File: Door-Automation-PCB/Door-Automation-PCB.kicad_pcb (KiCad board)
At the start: 2 copper layers, 139.3 x 70.4 mm, 10 parts, among them J1 Conn_01x15_Female, J2 Conn_01x15_Female, J3 Screw_Terminal_01x01, J4 Screw_Terminal_01x01, J5 Screw_Terminal_01x02, J6 Screw_Terminal_01x02, J7 Screw_Terminal_01x02, U1 ESP32-DEVKIT-V1, U2 buck_converter, U3 buck_converter

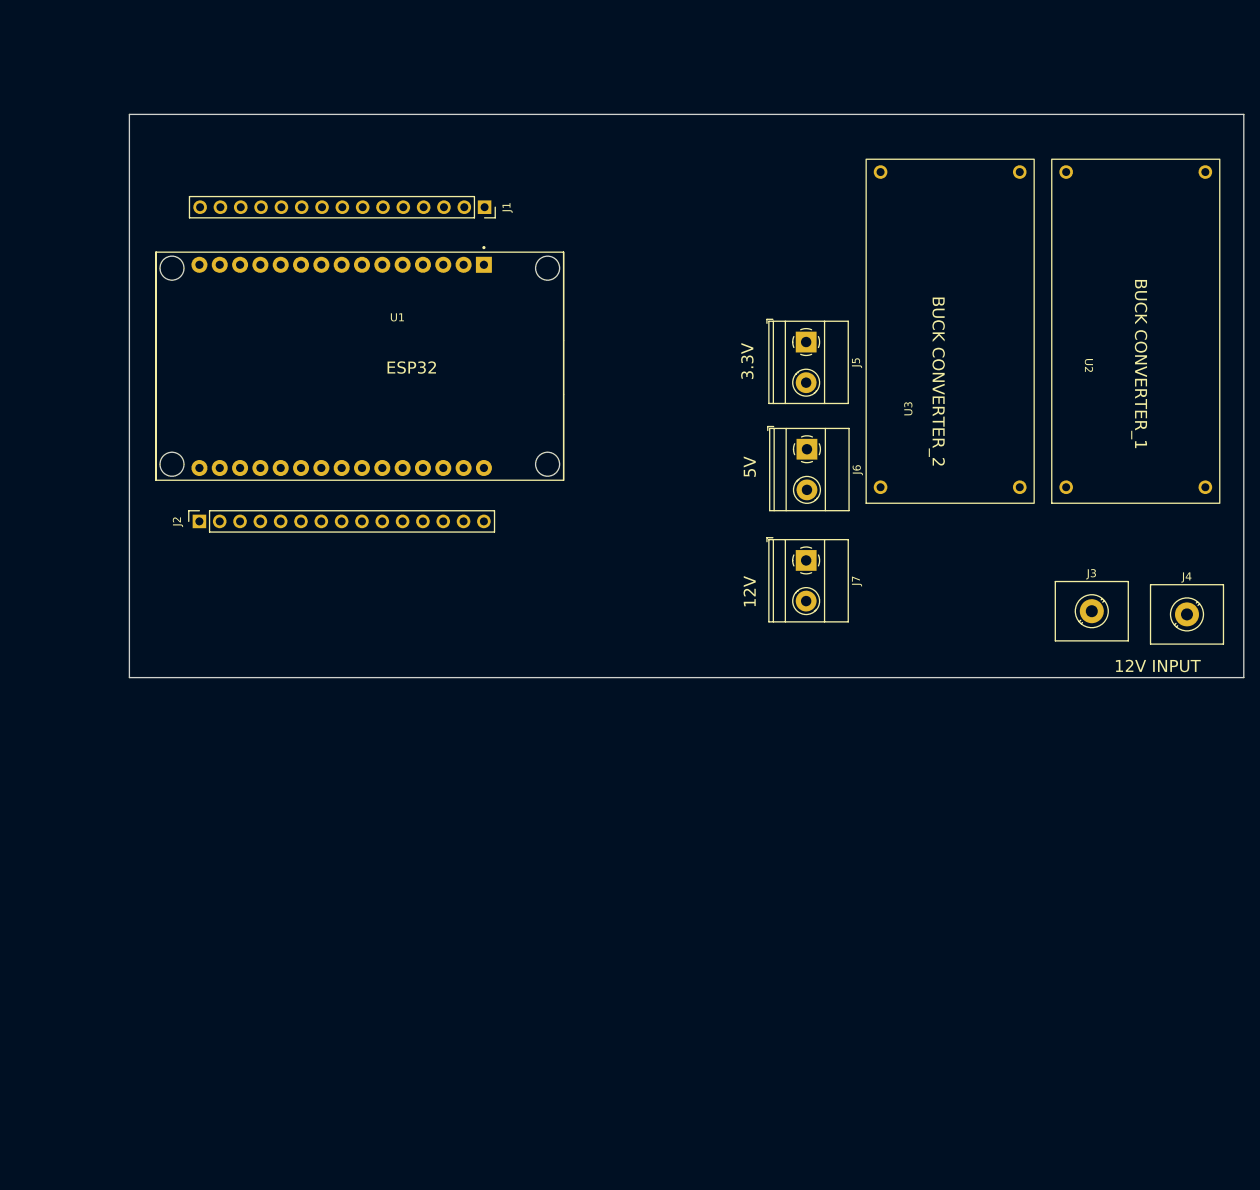
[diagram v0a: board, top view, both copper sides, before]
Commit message: added mosfet switch
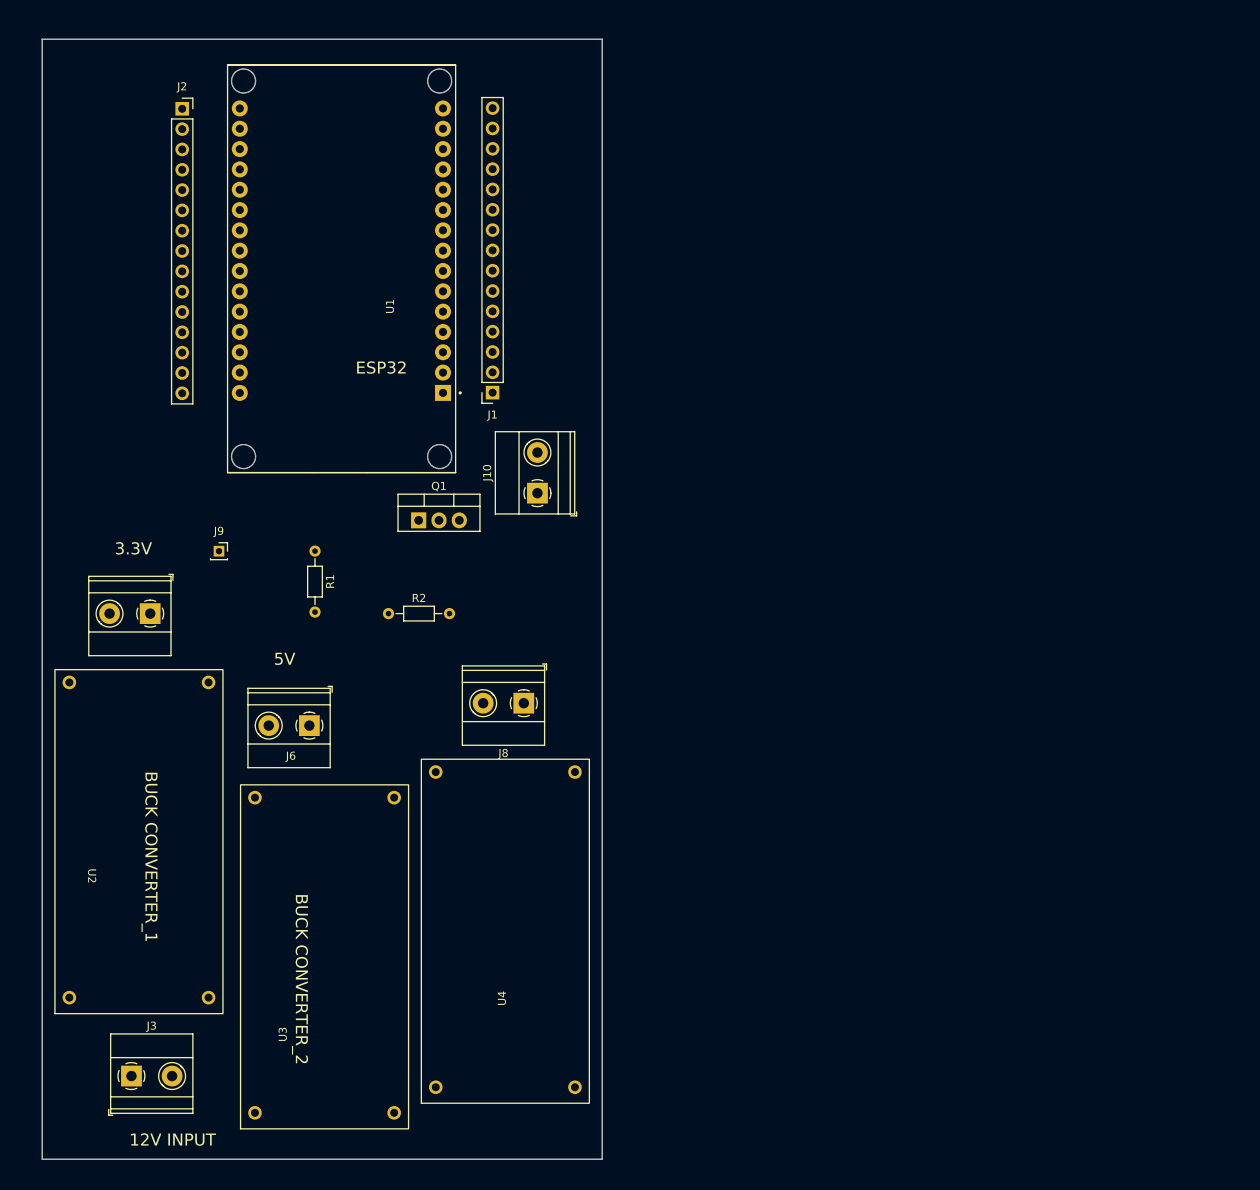
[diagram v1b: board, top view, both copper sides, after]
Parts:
- removed J4: Screw_Terminal_01x01, TerminalBlock_MetzConnect:TerminalBlock_MetzConnect_360271_1x01_Horizontal_ScrewM3.0_Boxed
- removed J7: Screw_Terminal_01x02, TerminalBlock_Phoenix:TerminalBlock_Phoenix_MKDS-1,5-2-5.08_1x02_P5.08mm_Horizontal
- added J10: Solenoid conn, TerminalBlock_Phoenix:TerminalBlock_Phoenix_MKDS-1,5-2-5.08_1x02_P5.08mm_Horizontal, F.Cu at (141.9, 96.7)
- added J8: 9V, TerminalBlock_Phoenix:TerminalBlock_Phoenix_MKDS-1,5-2-5.08_1x02_P5.08mm_Horizontal, F.Cu at (140.2, 123.0)
- added J9: D, Connector_PinSocket_2.00mm:PinSocket_1x01_P2.00mm_Vertical, F.Cu at (102.1, 104.0)
- added Q1: IRLZ34N, Package_TO_SOT_THT:TO-220-3_Vertical, F.Cu at (127.1, 100.1)
- added R1: 1K, Resistor_THT:R_Axial_DIN0204_L3.6mm_D1.6mm_P7.62mm_Horizontal, F.Cu at (114.1, 104.0)
- added R2: 1OK, Resistor_THT:R_Axial_DIN0204_L3.6mm_D1.6mm_P7.62mm_Horizontal, F.Cu at (123.3, 111.8)
- added U4: buck_converter, converters:buck_converter, F.Cu at (127.4, 173.0)
- J3: value Screw_Terminal_01x01 -> 12V_IN; footprint TerminalBlock_MetzConnect:TerminalBlock_MetzConnect_360271_1x01_Horizontal_ScrewM3.0_Boxed -> TerminalBlock_Phoenix:TerminalBlock_Phoenix_MKDS-1,5-2-5.08_1x02_P5.08mm_Horizontal
- J5: value Screw_Terminal_01x02 -> 3.3V
- J6: value Screw_Terminal_01x02 -> 5V
- moved U2 140.0 mm to (81.6, 161.8)
- moved J3 133.4 mm to (91.2, 169.6)
- moved U3 110.6 mm to (104.8, 176.2)
- moved J5 88.7 mm to (93.5, 111.8), turned to 180 degrees
- moved J6 71.1 mm to (113.4, 125.8), turned to 180 degrees
- moved J2 51.6 mm to (97.5, 48.7), turned to 0 degrees
- moved J1 23.2 mm to (136.3, 84.2), turned to 180 degrees
- moved U1 12.4 mm to (117.4, 68.7), turned to 180 degrees
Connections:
- net Net-(J5-Pad1) renamed /+3.3V
- net Net-(J6-Pad1) renamed /+5V
- J1 pad 2: Net-(J2-Pad14) -> /GND
- J2 pad 14: Net-(J2-Pad14) -> /GND
- J5 pad 2: Net-(J5-Pad2) -> /GND
- J6 pad 2: Net-(J5-Pad2) -> /GND
- U1 pad 2: Net-(J2-Pad14) -> /GND
- U1 pad 29: Net-(J2-Pad14) -> /GND
- U2 pad 1: Net-(J3-Pad1) -> Net-(J3-Pad2)
- U2 pad 2: Net-(J4-Pad1) -> Net-(J3-Pad1)
- U2 pad 4: Net-(J5-Pad2) -> /GND
- U3 pad 1: Net-(J3-Pad1) -> Net-(J3-Pad2)
- U3 pad 2: Net-(J4-Pad1) -> Net-(J3-Pad1)
- U3 pad 4: Net-(J5-Pad2) -> /GND
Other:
- board size 139.3 x 70.4 mm -> 70 x 140 mm
- board text removed: "12V"

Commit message: buck converter
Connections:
- J5 pad 1: /+3.3V -> /GND
- J5 pad 2: /GND -> /+3.3V
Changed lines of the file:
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@@
     (fp_circle (center 0 0) (end 1.5 0) (layer "F.Fab") (width 0.1) (fill none))
     (pad "1" thru_hole rect (at 0 0 180) (size 2.6 2.6) (drill 1.3) (layers *.Cu *.Mask)
-      (net 31 "/+3.3V") (pinfunction "Pin_1") (pintype "passive"))
+      (net 30 "/GND") (pinfunction "Pin_1") (pintype "passive"))
     (pad "2" thru_hole circle (at 5.08 0 180) (size 2.6 2.6) (drill 1.3) (layers *.Cu *.Mask)
-      (net 30 "/GND") (pinfunction "Pin_2") (pintype "passive"))
+      (net 31 "/+3.3V") (pinfunction "Pin_2") (pintype "passive"))
     (model "${KICAD6_3DMODEL_DIR}/TerminalBlock_Phoenix.3dshapes/TerminalBlock_Phoenix_MKDS-1,5-2-5.08_1x02_P5.08mm_Horizontal.wrl"
       (offset (xyz 0 0 0))

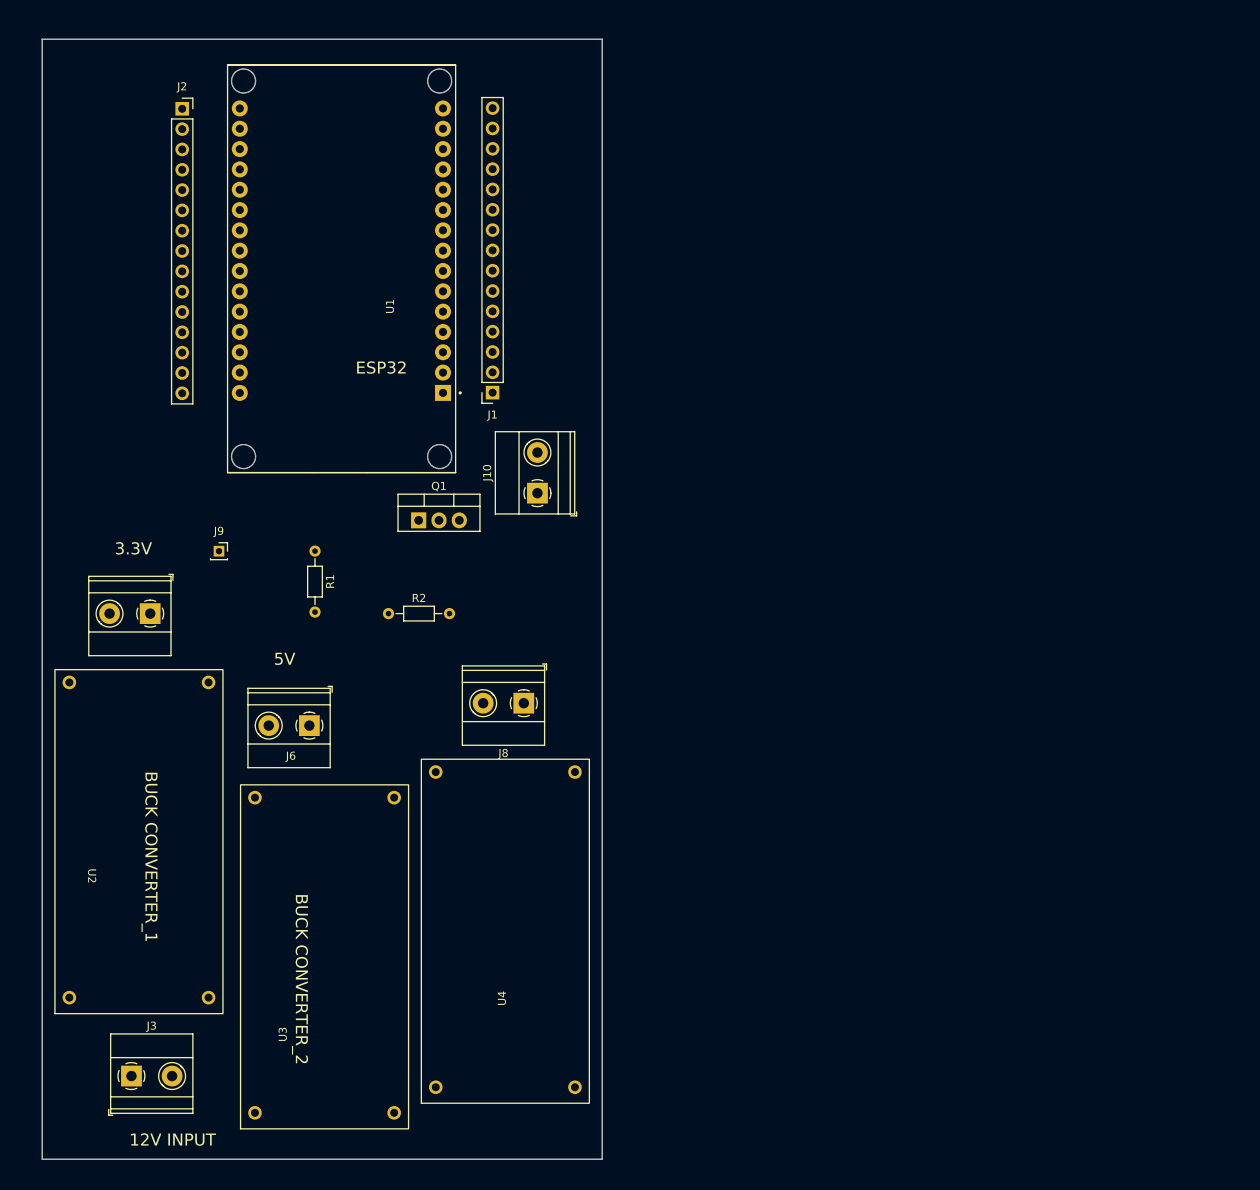
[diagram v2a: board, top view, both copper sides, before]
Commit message: added drill holes
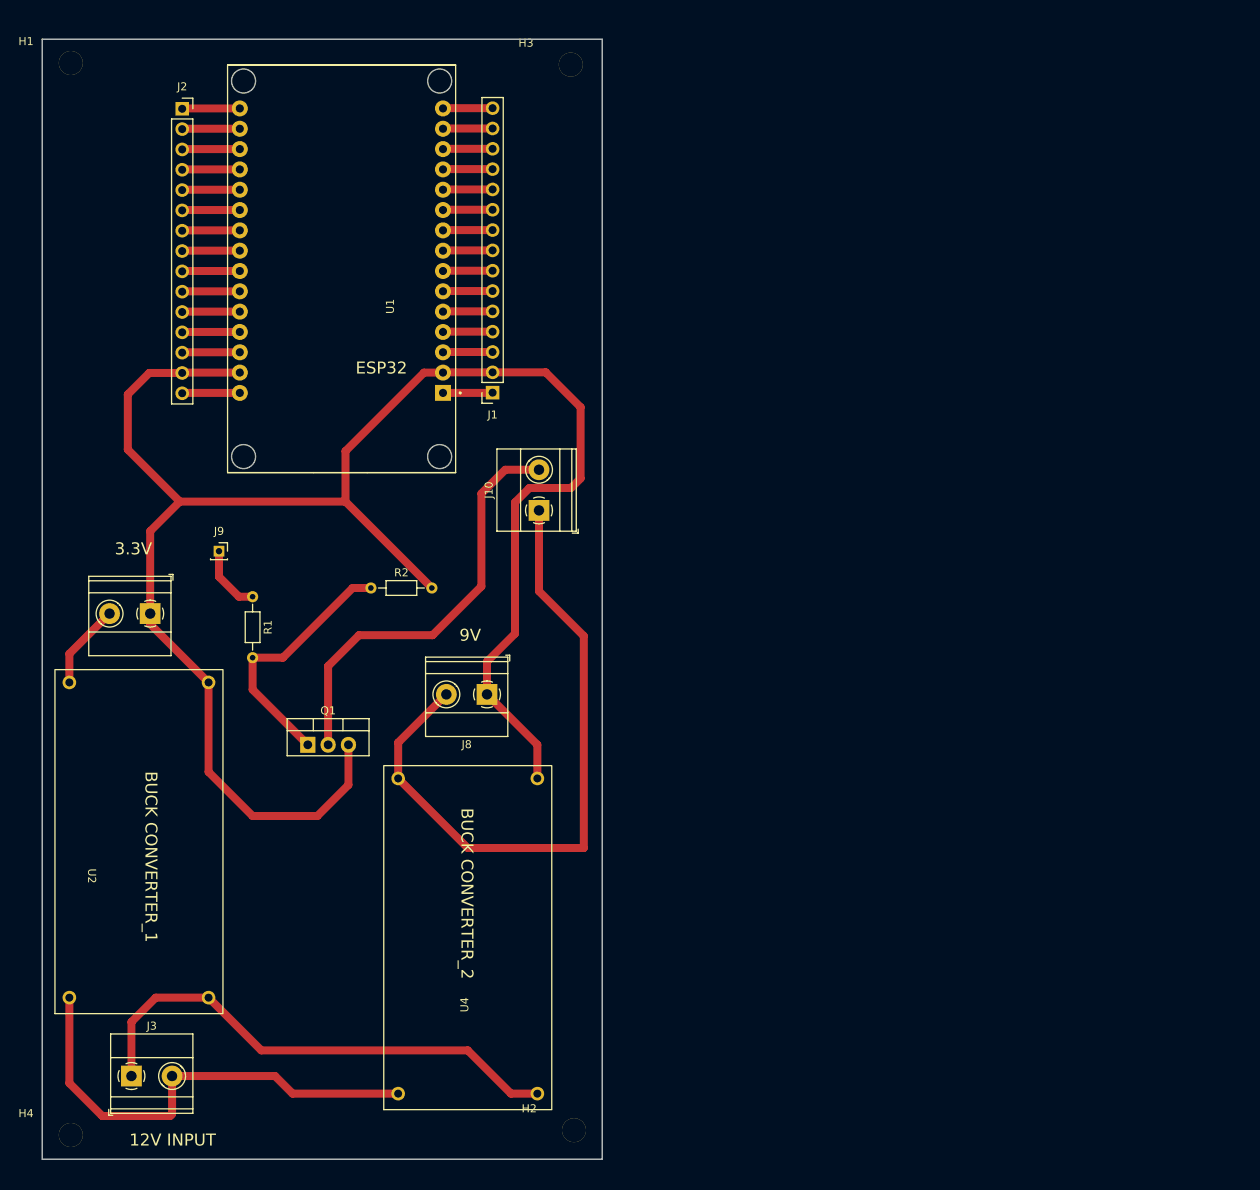
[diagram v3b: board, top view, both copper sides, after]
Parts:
- removed J6: 5V, TerminalBlock_Phoenix:TerminalBlock_Phoenix_MKDS-1,5-2-5.08_1x02_P5.08mm_Horizontal
- removed U3: buck_converter, converters:buck_converter
- added H1: hole, drill_hole:hole, F.Cu at (78.0, 40.8)
- added H2: hole, drill_hole:hole, F.Cu at (140.9, 174.2)
- added H3: hole, drill_hole:hole, F.Cu at (140.5, 41.0)
- added H4: hole, drill_hole:hole, F.Cu at (78.0, 174.8)
- moved Q1 31.3 mm to (113.2, 128.2)
- moved R1 9.66 mm to (106.3, 109.7)
- moved U4 4.77 mm to (122.7, 173.8)
- moved J8 4.73 mm to (135.6, 121.9)
- moved R2 3.88 mm to (121.1, 108.6)
- moved J10 2.16 mm to (142.1, 98.9)
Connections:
- J8 pad 1: /+9V -> /GND
- J8 pad 2: /GND -> /+9V
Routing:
- net /GND: track 0.00 -> 230.4 mm
- net /+9V: track 0.00 -> 84.3 mm
- net Net-(J3-Pad1): track 0.00 -> 63.7 mm
- net Net-(J3-Pad2): track 0.00 -> 59.3 mm
- net Net-(J10-Pad2): track 0.00 -> 53.2 mm
- net Net-(R1-Pad2): track 0.00 -> 32.1 mm
- net /+3.3V: track 0.00 -> 10.7 mm
- net Net-(R1-Pad1): track 0.00 -> 8.43 mm
- net Net-(J2-Pad9): track 0.00 -> 7.22 mm
- net Net-(J2-Pad8): track 0.00 -> 7.22 mm
- net Net-(J2-Pad6): track 0.00 -> 7.22 mm
- net Net-(J2-Pad5): track 0.00 -> 7.22 mm
- net Net-(J2-Pad4): track 0.00 -> 7.22 mm
- net Net-(J2-Pad3): track 0.00 -> 7.22 mm
- net Net-(J2-Pad2): track 0.00 -> 7.22 mm
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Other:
- board text added: "9V"
- board text removed: "5V"

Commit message: routed and added readme
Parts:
- H1, H2, H3, H4: value hole -> MountingHole; footprint drill_hole:hole -> MountingHole:MountingHole_2.5mm
- Q1: value IRLZ34N -> N-MOSFET
- actuator signal: renamed from J9
- moved H3 145.4 mm to (84.3, 175.1)
- moved H2 130.3 mm to (145.3, 44.0)
- moved H4 67.3 mm to (145.3, 175.1)
- moved J8 8.16 mm to (143.1, 125.0)
- moved H1 7.10 mm to (84.3, 44.0)
- moved U4 4.90 mm to (118.1, 175.5)
- moved Q1 4.89 mm to (108.8, 126.1)
- moved J3 3.14 mm to (94.3, 169.1)
- moved J10 2.29 mm to (139.9, 99.5)
- renumbered U1 to ESP32
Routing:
- net /+9V: track 84.3 -> 53.1 mm
- net /GND: track 230.4 -> 215.5 mm
- net Net-(J3-Pad2): track 59.3 -> 51.3 mm
- net Net-(J3-Pad1): track 63.7 -> 57.0 mm
- net Net-(Q1-Pad1): track 32.1 -> 28.4 mm
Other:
- board text added: "+"
- board text added: "-"
- board text removed: "12V INPUT"
- board text removed: "9V"
- board text removed: "BUCK CONVERTER_1"
- board text removed: "BUCK CONVERTER_2"
- board text removed: "ESP32"
